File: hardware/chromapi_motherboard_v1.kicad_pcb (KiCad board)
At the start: 2 copper layers, 139 parts, among them J1 Battery Input, J10 Conn_FSR_TopLeft, J11 Conn_FSR_TopRight, J12 Conn_FSR_BotLeft, J13 Conn_FSR_BotRight, J14 RPI_Connector, J2 Power Switch, J3 USB_C_Receptacle_USB2.0_14P, J4 Conn_ST_STDC14, J5 Conn_01x03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

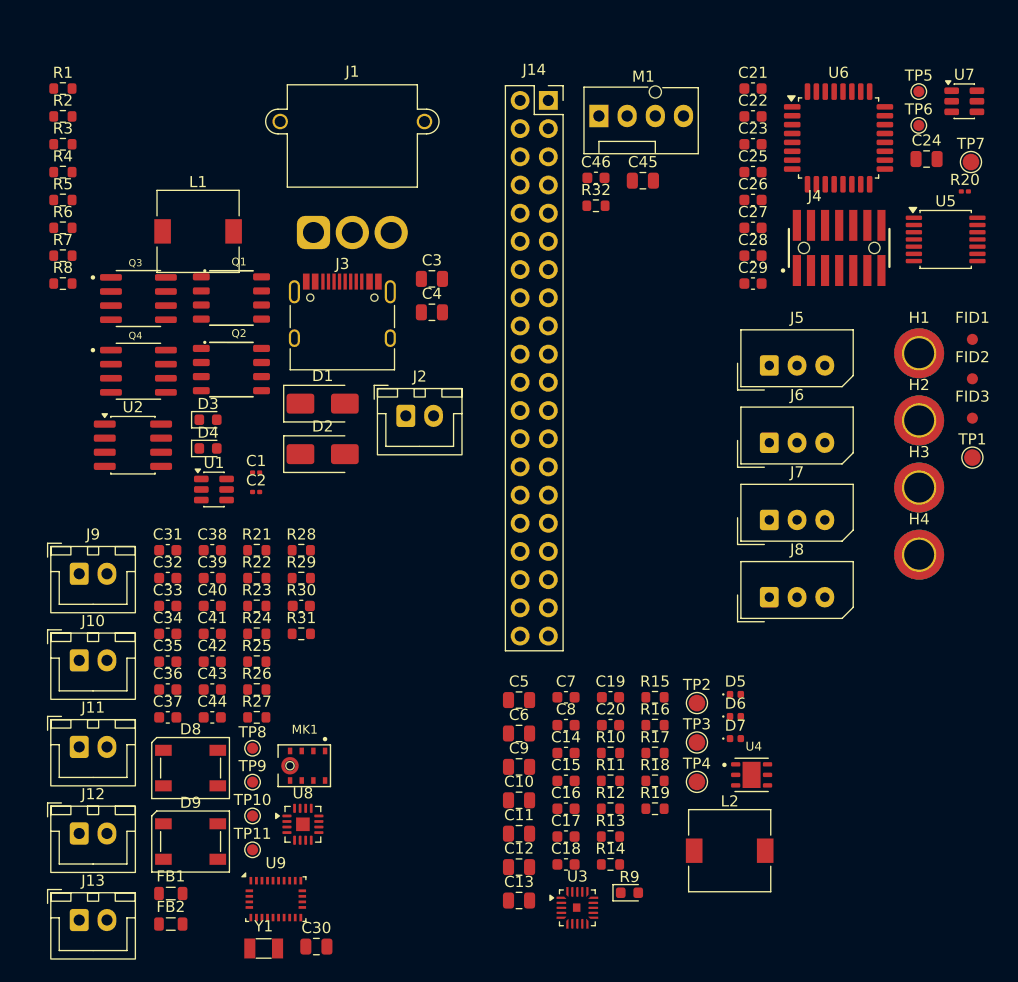
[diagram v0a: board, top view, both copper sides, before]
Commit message: Modyfing components footprints
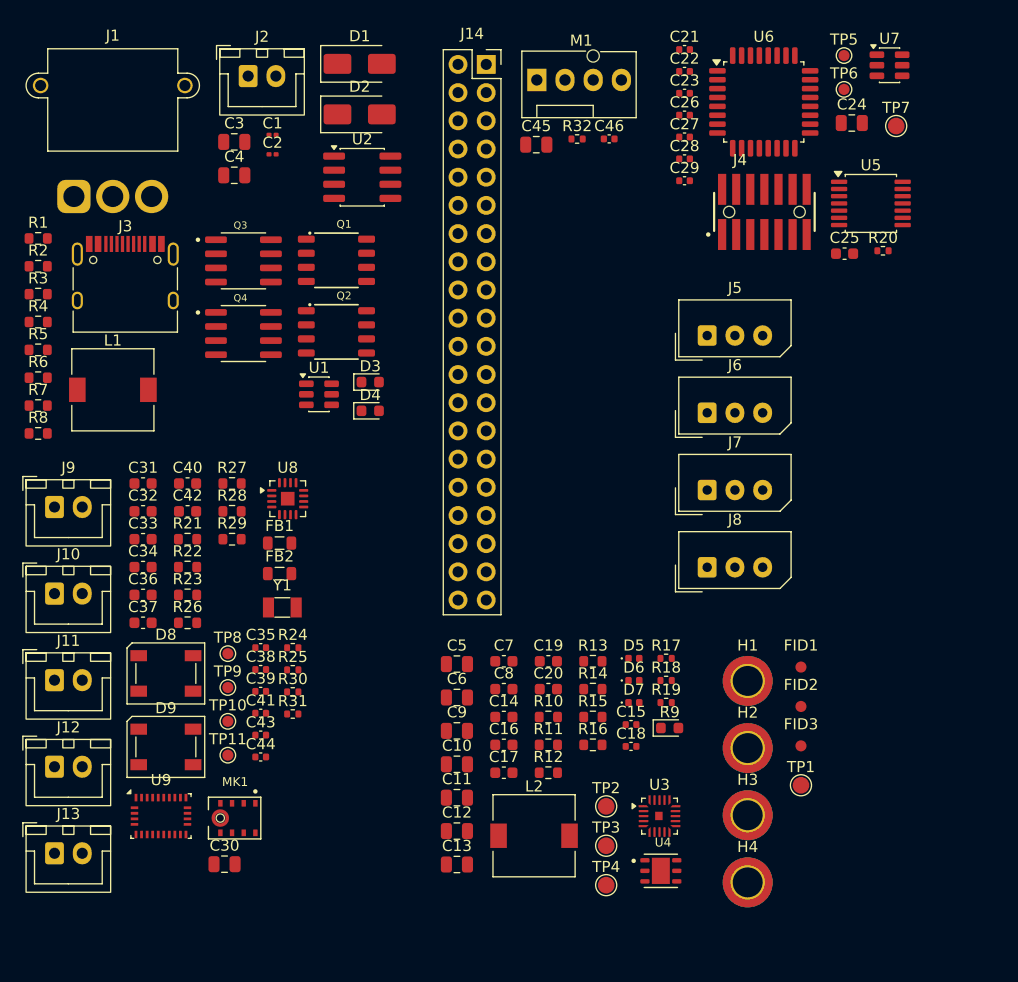
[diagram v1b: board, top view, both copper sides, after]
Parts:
- C15, C18, C21, C22, C23, C26, C27, C28, C29, C35, C38, C39, C41, C43, C44, C46: footprint Capacitor_SMD:C_0603_1608Metric -> Capacitor_SMD:C_0402_1005Metric
- R17, R18, R19, R24, R25, R31, R32: footprint Resistor_SMD:R_0603_1608Metric -> Resistor_SMD:R_0402_1005Metric
- R20: footprint Capacitor_SMD:C_0201_0603Metric -> Resistor_SMD:R_0402_1005Metric
- R30: footprint Capacitor_SMD:C_0603_1608Metric -> Resistor_SMD:R_0402_1005Metric
- moved J2 33.8 mm to (38.5, 21.0)
- moved H2 33.3 mm to (83.5, 81.5)
- moved H3 33.3 mm to (83.5, 87.6)
- moved H4 33.3 mm to (83.5, 93.6)
- moved FID2 33.3 mm to (88.3, 77.8)
- moved FID3 33.3 mm to (88.3, 81.3)
- moved H1 33.3 mm to (83.5, 75.5)
- moved FID1 33.3 mm to (88.3, 74.2)
- moved TP1 33.3 mm to (88.3, 84.9)
- moved FB1 33.1 mm to (41.4, 63.1)
- moved FB2 33.1 mm to (41.4, 65.8)
- moved U2 31.8 mm to (48.8, 30.1)
- moved D1 30.8 mm to (48.6, 19.9)
- moved D2 30.8 mm to (48.6, 24.4)
- moved Y1 30.8 mm to (41.6, 68.9)
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
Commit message: minor fixes
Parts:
- C14: footprint Capacitor_SMD:C_0603_1608Metric -> Capacitor_SMD:C_0402_1005Metric
- J14: moved to B.Cu
- J5: value Conn_01x03 -> Conn_TopLeft
- J6: value Conn_01x03 -> Conn_TopRight
- J7: value Conn_01x03 -> Conn_BotLeft
- J8: value Conn_01x03 -> Conn_BotRight
- R10: footprint Resistor_SMD:R_0603_1608Metric -> Resistor_SMD:R_0402_1005Metric_Pad0.72x0.64mm_HandSolder
- moved J14 98.7 mm to (154.0, 50.0), turned to 90 degrees
- moved J6 91.1 mm to (171.0, 50.0), turned to 180 degrees
- moved J8 90.6 mm to (166.0, 93.5)
- moved C13 90.6 mm to (147.4, 82.0), turned to -90 degrees
- moved C8 88.5 mm to (149.9, 82.0), turned to -90 degrees
- moved C12 87.3 mm to (144.4, 82.0), turned to -90 degrees
- moved C11 84.2 mm to (141.4, 82.0), turned to -90 degrees
- moved C10 81.1 mm to (138.4, 82.0), turned to -90 degrees
- moved C9 78.1 mm to (135.4, 82.0), turned to -90 degrees
- moved R11 73.4 mm to (135.2, 58.0)
- moved R12 73.4 mm to (135.2, 60.5)
- moved C17 65.3 mm to (124.7, 67.0)
- moved C16 65.3 mm to (124.7, 64.5)
- moved L2 65.1 mm to (128.7, 80.0)
- moved C14 64.0 mm to (125.5, 75.0), turned to 180 degrees
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
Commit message: Replacing AO4406A by PSMN1R5-30YLC
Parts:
- added Q1: PSMN1R5-30YL, Package_TO_SOT_SMD:LFPAK56, F.Cu at (60.9, 41.3)
- added Q2: PSMN1R5-30YL, Package_TO_SOT_SMD:LFPAK56, F.Cu at (60.9, 48.0)
- J1: footprint Connector_AMASS:AMASS_MR30PW-M_1x03_P3.50mm_Horizontal -> Connector_JST:JST_XH_B3B-XH-AM_1x03_P2.50mm_Vertical
- moved J1 5.48 mm to (19.5, 27.5)

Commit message: Component spacing
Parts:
- removed the Q1 at (46.5, 37.6)
- removed the Q2 at (46.5, 44.0)
- moved U9 206.2 mm to (236.8, 80.7)
- moved C40 203.7 mm to (236.7, 61.3)
- moved C42 203.7 mm to (236.7, 63.8)
- moved R22 203.7 mm to (236.7, 68.9)
- moved R26 203.7 mm to (236.7, 73.9)
- moved C36 203.7 mm to (232.7, 71.4)
- moved C37 203.7 mm to (232.7, 73.9)
- moved R27 203.7 mm to (240.7, 61.3)
- moved R28 203.7 mm to (240.7, 63.8)
- moved R29 203.7 mm to (240.7, 66.3)
- moved Y1 203.7 mm to (245.2, 72.5)
- moved FB1 197.6 mm to (226.8, 131.2)
- moved FB2 197.6 mm to (226.8, 134.0)
- moved J9 197.6 mm to (206.5, 128.0)
- moved R21 197.6 mm to (218.5, 130.9)
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
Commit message: updating component placcement
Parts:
- C1, C2: footprint Capacitor_SMD:C_0201_0603Metric -> Capacitor_SMD:C_0402_1005Metric
- R1, R2, R3: footprint Resistor_SMD:R_0603_1608Metric -> Resistor_SMD:R_0402_1005Metric
- moved TP1 164.4 mm to (248.0, 124.0)
- moved C2 93.5 mm to (33.0, 28.0), turned to 90 degrees
- moved C1 91.8 mm to (34.5, 28.0), turned to 90 degrees
- moved R3 90.3 mm to (46.0, 28.5), turned to -90 degrees
- moved R2 86.2 mm to (31.5, 28.0), turned to -90 degrees
- moved U1 85.9 mm to (40.0, 28.0), turned to 180 degrees
- moved R1 84.2 mm to (36.0, 28.0), turned to -90 degrees
- moved Q2 80.8 mm to (44.7, 37.1), turned to 180 degrees
- moved Q1 73.5 mm to (36.3, 37.0)
- moved C32 48.7 mm to (206.9, 109.7)
- moved MK1 40.3 mm to (206.0, 106.5)
- moved Y1 40.0 mm to (205.2, 72.8), turned to 90 degrees
- moved C30 39.9 mm to (219.8, 100.6), turned to 90 degrees
- moved FB2 39.8 mm to (212.2, 97.0), turned to 180 degrees
- moved C34 36.9 mm to (220.5, 97.0)
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
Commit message: updating component placement
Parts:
- moved R14 22.5 mm to (121.5, 83.3), turned to 90 degrees
- moved C25 22.2 mm to (146.7, 42.0)
- moved C26 18.5 mm to (146.5, 40.5)
- moved R16 18.5 mm to (119.5, 83.5), turned to -90 degrees
- moved J4 8.32 mm to (158.5, 33.5), turned to 90 degrees
- moved C22 7.30 mm to (139.0, 30.0), turned to 180 degrees
- moved C27 6.94 mm to (118.0, 36.0), turned to -90 degrees
- moved TP7 6.26 mm to (106.0, 42.5)
- moved C23 3.96 mm to (139.0, 28.5), turned to 180 degrees
- moved C28 2.93 mm to (122.0, 34.0)
- moved C24 2.29 mm to (139.0, 26.0), turned to 180 degrees
- moved R20 1.50 mm to (142.0, 28.5), turned to 180 degrees

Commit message: Updating component placement
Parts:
- C10, C11, C12, C13, C5, C6, C9: footprint Capacitor_SMD:C_0805_2012Metric -> Capacitor_SMD:C_1206_3216Metric
- C24, C3, C4, C45: footprint Capacitor_SMD:C_0805_2012Metric -> Capacitor_SMD:CP_Elec_4x4.5
- moved R11 81.3 mm to (124.1, 138.5), turned to 90 degrees
- moved R13 79.0 mm to (121.6, 138.5), turned to -90 degrees
- moved R12 78.5 mm to (135.1, 139.0), turned to 180 degrees
- moved C16 74.0 mm to (126.6, 138.5), turned to -90 degrees
- moved R15 74.0 mm to (131.8, 139.0)
- moved C17 71.5 mm to (112.6, 137.5), turned to 180 degrees
- moved R9 70.7 mm to (112.3, 131.5)
- moved R14 55.4 mm to (116.6, 138.5)
- moved R16 55.0 mm to (119.6, 138.5)
- moved C40 54.2 mm to (258.1, 60.3)
- moved R22 54.2 mm to (266.6, 62.1)
- moved R26 54.2 mm to (264.3, 59.1)
- moved R27 54.2 mm to (261.3, 59.1)
- moved Y1 54.2 mm to (258.6, 63.1)
- moved C36 54.2 mm to (261.6, 67.1)
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
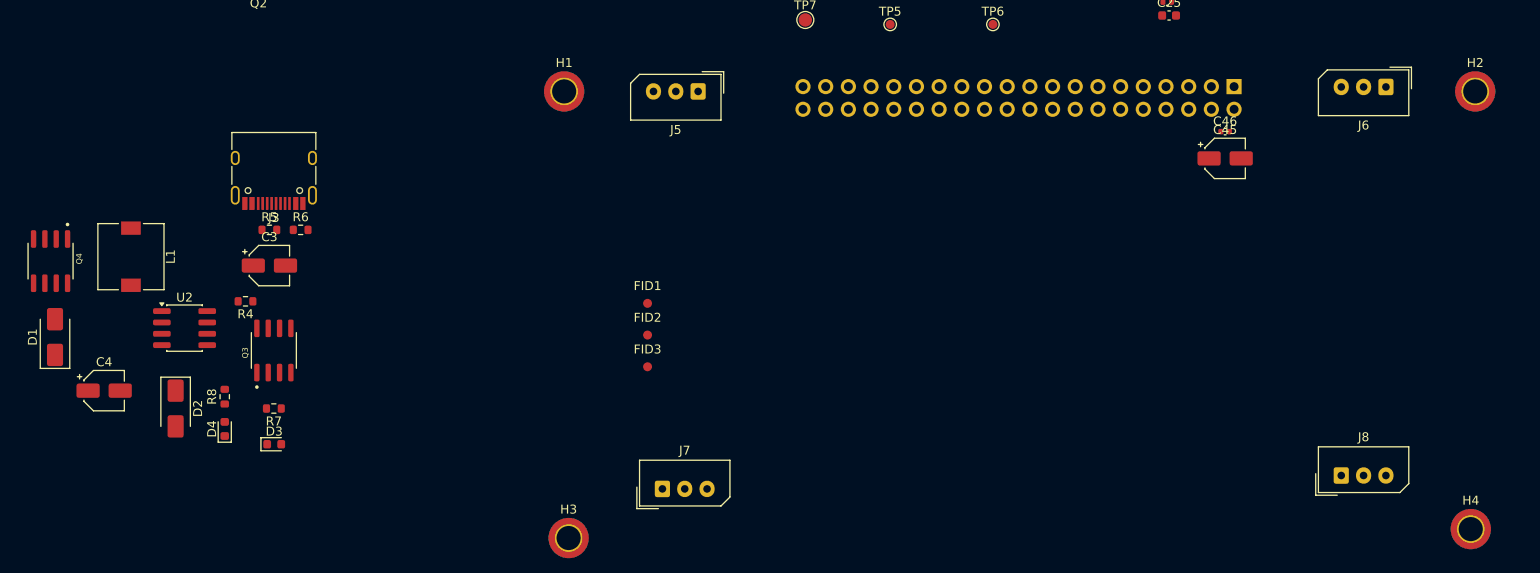
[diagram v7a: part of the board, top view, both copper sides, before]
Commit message: adding chromapi logo to library
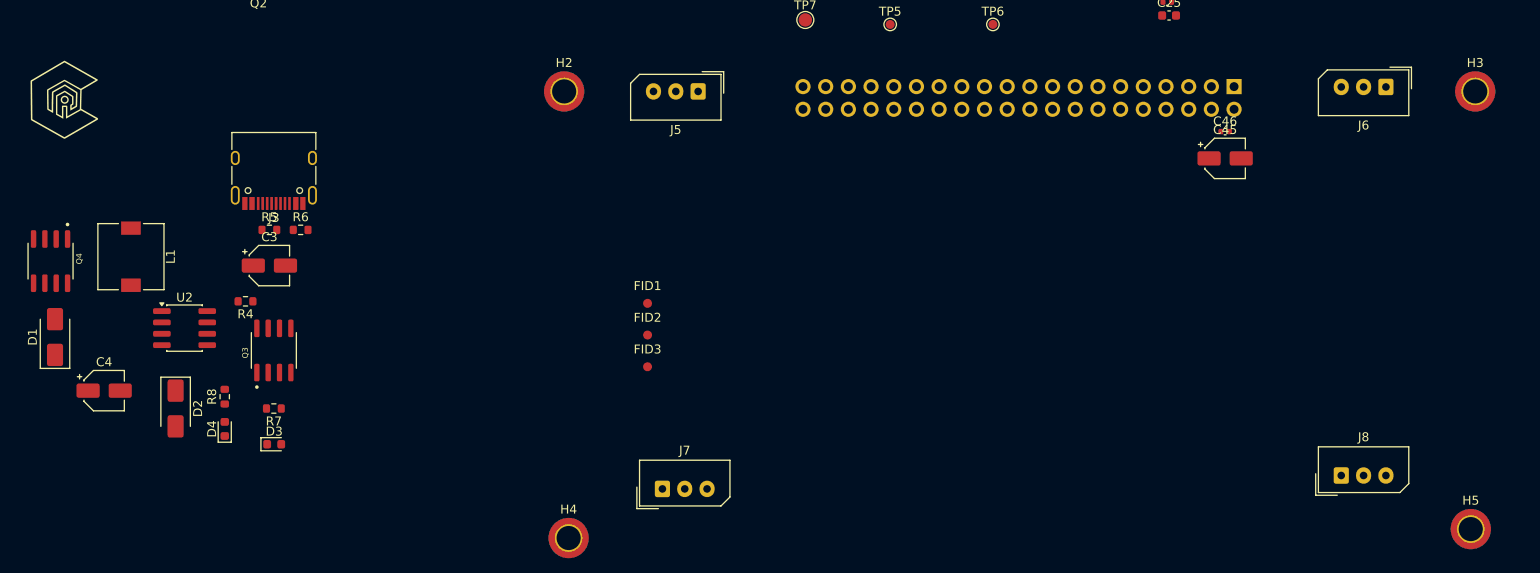
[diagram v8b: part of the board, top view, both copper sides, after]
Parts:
- added H1: ~, Chromapi_FP:chromapi_logo, F.Cu at (23.0, 51.5)
- renumbered H1 to H2, H2 to H3, H3 to H4, H4 to H5
